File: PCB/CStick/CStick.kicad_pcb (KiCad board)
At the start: 2 copper layers, 39.1 x 31.5 mm, 7 parts, among them J1 Conn_01x04_Male, U1 Stickbox_Assembly

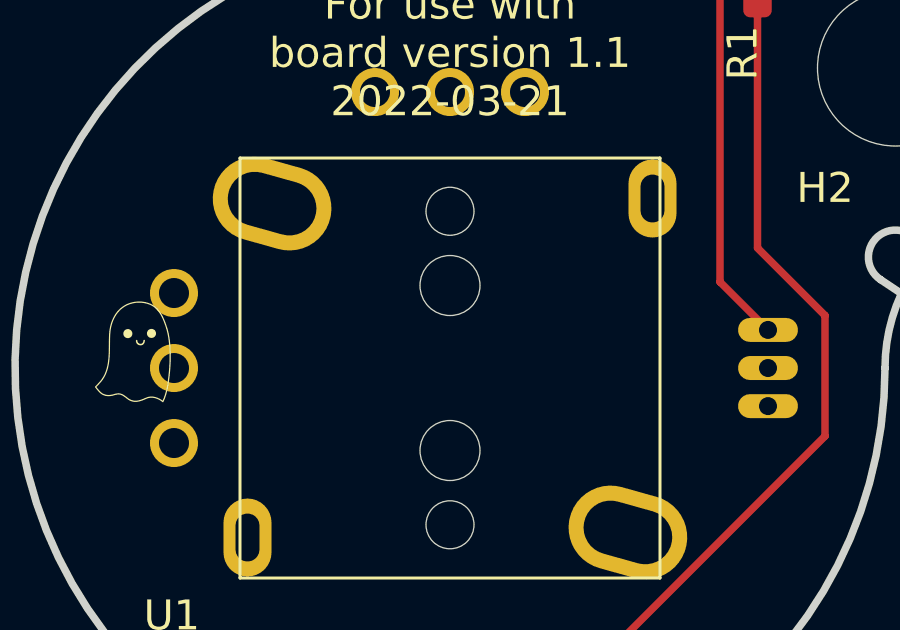
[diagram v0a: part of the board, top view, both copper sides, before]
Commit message: Added the missing mounting holes to the c-stick
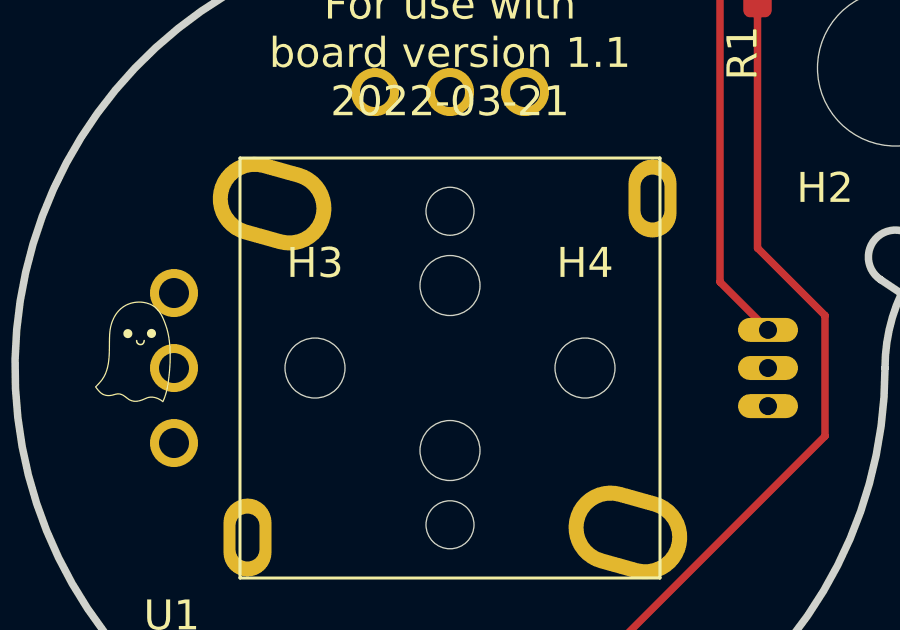
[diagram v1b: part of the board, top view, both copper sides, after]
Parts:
- added H3: MountingHole, Gamecube MB:MountingHole_2.0mm, F.Cu at (145.5, 100.0)
- added H4: MountingHole, Gamecube MB:MountingHole_2.0mm, F.Cu at (154.5, 100.0)
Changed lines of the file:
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@@
     )
+  )
+  (footprint "Gamecube MB:MountingHole_2.0mm" (layer "F.Cu")
+    (at 145.5 100)
+    (descr "Mounting Hole 2.5mm, no annular")
+    (tags "mounting hole 2.5mm no annular")
+    (property "Sheetfile" "CStick.kicad_sch")
+    (property "Sheetname" "")
+    (attr exclude_from_pos_files)
+    (fp_text reference "H3" (at 0 -3.5) (layer "F.SilkS")
+      (effects (font (size 1 1) (thickness 0.15)))
+    )
+    (fp_text value "MountingHole" (at 0 3.5) (layer "F.Fab")
+      (effects (font (size 1 1) (thickness 0.15)))
+    )
+    (fp_text user "${REFERENCE}" (at 0.3 0) (layer "F.Fab")
+      (effects (font (size 1 1) (thickness 0.15)))
+    )
+    (fp_circle (center 0 0) (end 2.5 0) (layer "Cmts.User") (width 0.15) (fill none))
+    (fp_circle (center 0 0) (end 1.2 0) (layer "F.CrtYd") (width 0.05) (fill none))
+    (pad "" np_thru_hole circle locked (at 0 0) (size 2 2) (drill 2) (layers *.Cu *.Mask))
   )
   (footprint "Gamecube MB:MountingHole_5.2mm" (layer "F.Cu")
@@
       (net 1 "VCC") (pinfunction "P1YV") (pintype "unspecified"))
   )
+  (footprint "Gamecube MB:MountingHole_2.0mm" (layer "F.Cu")
+    (at 154.5 100)
+    (descr "Mounting Hole 2.5mm, no annular")
+    (tags "mounting hole 2.5mm no annular")
+    (property "Sheetfile" "CStick.kicad_sch")
+    (property "Sheetname" "")
+    (attr exclude_from_pos_files)
+    (fp_text reference "H4" (at 0 -3.5) (layer "F.SilkS")
+      (effects (font (size 1 1) (thickness 0.15)))
+    )
+    (fp_text value "MountingHole" (at 0 3.5) (layer "F.Fab")
+      (effects (font (size 1 1) (thickness 0.15)))
+    )
+    (fp_text user "${REFERENCE}" (at 0.3 0) (layer "F.Fab")
+      (effects (font (size 1 1) (thickness 0.15)))
+    )
+    (fp_circle (center 0 0) (end 2.5 0) (layer "Cmts.User") (width 0.15) (fill none))
+    (fp_circle (center 0 0) (end 1.2 0) (layer "F.CrtYd") (width 0.05) (fill none))
+    (pad "" np_thru_hole circle locked (at 0 0) (size 2 2) (drill 2) (layers *.Cu *.Mask))
+  )
   (gr_circle (center 150 100) (end 162 100) (layer "Dwgs.User") (width 0.1) (fill none))
